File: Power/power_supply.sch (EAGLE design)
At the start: 7 parts

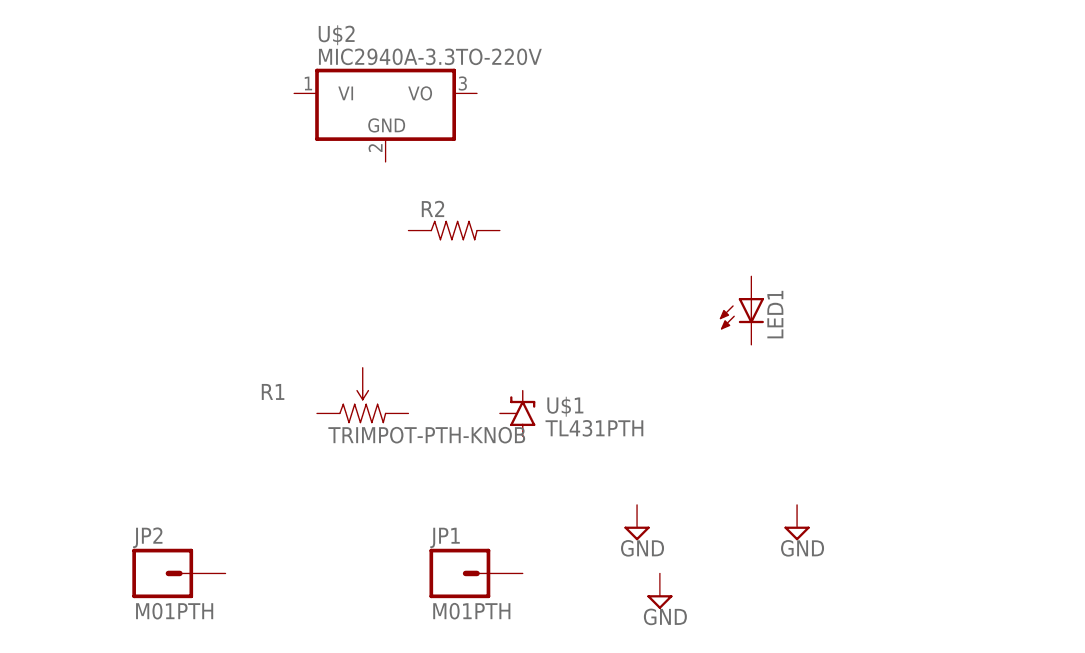
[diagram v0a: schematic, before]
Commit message: Changes to the Power Supply
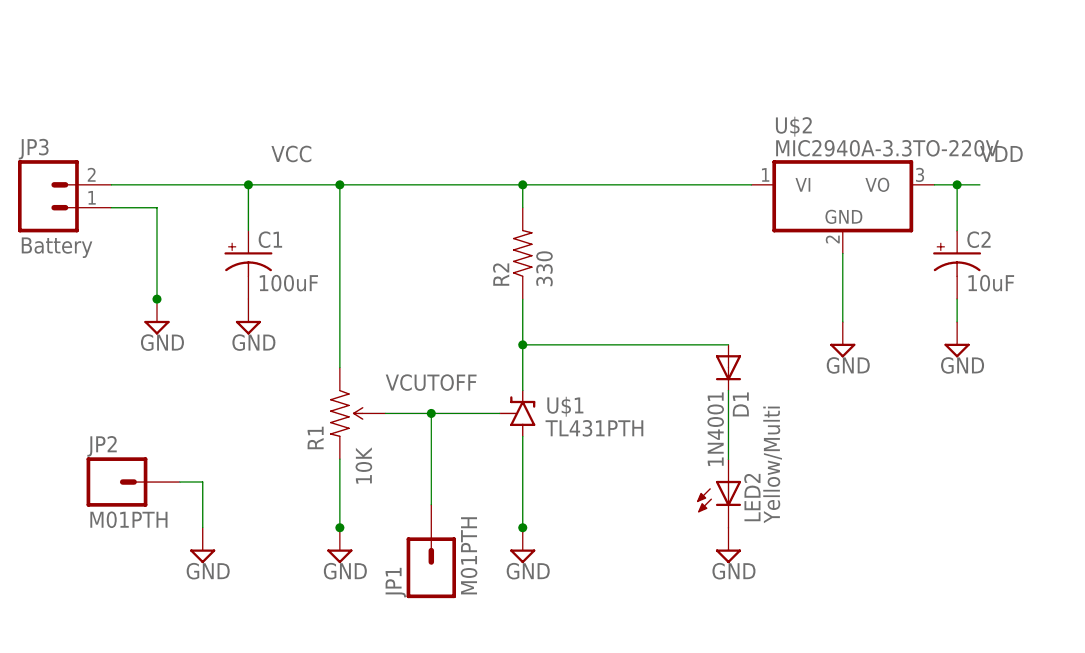
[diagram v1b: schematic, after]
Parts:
- removed LED1: (no value), SparkFun:LED10MM2
- added C1: 100uF, rcl:CPOL-USE3.5-8
- added C2: 10uF, rcl:CPOL-USE2.5-5
- added D1: 1N4001, diode:1N4004
- added JP3: Battery, SparkFun:M02PTH
- added LED2: Yellow/Multi, SparkFun:LED5MM
- R1: value TRIMPOT-PTH-KNOB -> 10K
- R2: value (none) -> 330
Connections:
- new net GND: C1.-, C2.-, JP2.1, JP3.1, LED2.C, R1.CW, U$1.A, U$2.GND
- new net N$1: D1.C, LED2.A
- new net N$2: D1.A, R2.1, U$1.C
- new net VCC: C1.+, JP3.2, R1.CCW, R2.2, U$2.VI
- new net VCUTOFF: JP1.1, R1.WIPER, U$1.R
- new net VDD: C2.+, U$2.VO
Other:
- moved on the sheet: JP1, JP2, R1, R2, U$2
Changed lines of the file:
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@@
 <layer number="97" name="Info" color="7" fill="1" visible="yes" active="yes"/>
 <layer number="98" name="Guide" color="6" fill="1" visible="yes" active="yes"/>
+<layer number="99" name="SpiceOrder" color="5" fill="1" visible="yes" active="yes"/>
 <layer number="100" name="Muster" color="7" fill="1" visible="yes" active="yes"/>
 <layer number="101" name="Patch_Top" color="7" fill="1" visible="yes" active="yes"/>
@@
 <parts>
 <part name="U$1" library="SparkFun" deviceset="TL431" device="PTH"/>
-<part name="R1" library="SparkFun" deviceset="TRIMPOT" device="-PTH-KNOB"/>
-<part name="R2" library="SparkFun" deviceset="RESISTOR" device="AXIAL-0.3"/>
+<part name="R1" library="SparkFun" deviceset="TRIMPOT" device="-PTH-KNOB" value="10K"/>
+<part name="R2" library="SparkFun" deviceset="RESISTOR" device="AXIAL-0.3" value="330"/>
 <part name="JP1" library="SparkFun" deviceset="M01" device="PTH"/>
 <part name="JP2" library="SparkFun" deviceset="M01" device="PTH"/>
-<part name="LED1" library="SparkFun" deviceset="LED" device="10MM2"/>
 <part name="SUPPLY1" library="supply2" deviceset="GND" device=""/>
 <part name="SUPPLY2" library="supply2" deviceset="GND" device=""/>
-<part name="SUPPLY3" library="supply2" deviceset="GND" device=""/>
 <part name="U$2" library="SparkFun" deviceset="MIC2940A-3.3" device="TO-220V"/>
+<part name="SUPPLY4" library="supply2" deviceset="GND" device=""/>
+<part name="SUPPLY5" library="supply2" deviceset="GND" device=""/>
+<part name="JP3" library="SparkFun" deviceset="M02" device="PTH" value="Battery"/>
+<part name="SUPPLY6" library="supply2" deviceset="GND" device=""/>
+<part name="SUPPLY7" library="supply2" deviceset="GND" device=""/>
+<part name="C1" library="rcl" deviceset="CPOL-US" device="E3.5-8" value="100uF"/>
+<part name="C2" library="rcl" deviceset="CPOL-US" device="E2.5-5" value="10uF"/>
+<part name="SUPPLY8" library="supply2" deviceset="GND" device=""/>
+<part name="SUPPLY9" library="supply2" deviceset="GND" device=""/>
+<part name="D1" library="diode" deviceset="1N4004" device="" value="1N4001"/>
+<part name="LED2" library="SparkFun" deviceset="LED" device="5MM" value="Yellow/Multi"/>
 </parts>
 <sheets>
@@
 <instances>
 <instance part="U$1" gate="G$1" x="25.4" y="12.7"/>
-<instance part="R1" gate="R?" x="7.62" y="12.7"/>
-<instance part="R2" gate="G$1" x="17.78" y="33.02"/>
-<instance part="JP1" gate="G$1" x="17.78" y="-5.08"/>
-<instance part="JP2" gate="G$1" x="-15.24" y="-5.08"/>
-<instance part="LED1" gate="G$1" x="50.8" y="25.4"/>
-<instance part="SUPPLY1" gate="GND" x="38.1" y="0"/>
-<instance part="SUPPLY2" gate="GND" x="40.64" y="-7.62"/>
-<instance part="SUPPLY3" gate="GND" x="55.88" y="0"/>
-<instance part="U$2" gate="G$1" x="10.16" y="48.26"/>
+<instance part="R1" gate="R?" x="5.08" y="12.7" smashed="yes" rot="R270">
+<attribute name="NAME" x="1.4986" y="11.43" size="1.778" layer="95" rot="R270"/>
+<attribute name="VALUE" x="6.858" y="8.89" size="1.778" layer="96" rot="R270"/>
+</instance>
+<instance part="R2" gate="G$1" x="25.4" y="30.48" rot="R90"/>
+<instance part="JP1" gate="G$1" x="15.24" y="-5.08" rot="R90"/>
+<instance part="JP2" gate="G$1" x="-20.32" y="5.08"/>
+<instance part="SUPPLY1" gate="GND" x="-10.16" y="-2.54"/>
+<instance part="SUPPLY2" gate="GND" x="5.08" y="-2.54"/>
+<instance part="U$2" gate="G$1" x="60.96" y="38.1"/>
+<instance part="SUPPLY4" gate="GND" x="25.4" y="-2.54"/>
+<instance part="SUPPLY5" gate="GND" x="48.26" y="-2.54"/>
+<instance part="JP3" gate="G$1" x="-27.94" y="35.56"/>
+<instance part="SUPPLY6" gate="GND" x="-15.24" y="22.86"/>
+<instance part="SUPPLY7" gate="GND" x="60.96" y="20.32"/>
+<instance part="C1" gate="G$1" x="-5.08" y="30.48"/>
+<instance part="C2" gate="G$1" x="73.66" y="30.48"/>
+<instance part="SUPPLY8" gate="GND" x="-5.08" y="22.86"/>
+<instance part="SUPPLY9" gate="GND" x="73.66" y="20.32"/>
+<instance part="D1" gate="1" x="48.26" y="17.78" rot="R270"/>
+<instance part="LED2" gate="G$1" x="48.26" y="5.08"/>
 </instances>
 <busses>
 </busses>
 <nets>
+<net name="GND" class="0">
+<segment>
+<pinref part="JP2" gate="G$1" pin="1"/>
+<pinref part="SUPPLY1" gate="GND" pin="GND"/>
+<wire x1="-12.7" y1="5.08" x2="-10.16" y2="5.08" width="0.1524" layer="91"/>
+<wire x1="-10.16" y1="5.08" x2="-10.16" y2="0" width="0.1524" layer="91"/>
+</segment>
+<segment>
+<pinref part="SUPPLY4" gate="GND" pin="GND"/>
+<pinref part="U$1" gate="G$1" pin="A"/>
+<wire x1="25.4" y1="10.16" x2="25.4" y2="0" width="0.1524" layer="91"/>
+<junction x="25.4" y="0"/>
+</segment>
+<segment>
+<pinref part="R1" gate="R?" pin="CW"/>
+<pinref part="SUPPLY2" gate="GND" pin="GND"/>
+<wire x1="5.08" y1="7.62" x2="5.08" y2="0" width="0.1524" layer="91"/>
+<junction x="5.08" y="0"/>
+</segment>
+<segment>
+<pinref part="JP3" gate="G$1" pin="1"/>
+<wire x1="-20.32" y1="35.56" x2="-15.24" y2="35.56" width="0.1524" layer="91"/>
+<pinref part="SUPPLY6" gate="GND" pin="GND"/>
+<wire x1="-15.24" y1="35.56" x2="-15.24" y2="25.4" width="0.1524" layer="91"/>
+<junction x="-15.24" y="25.4"/>
+</segment>
+<segment>
+<pinref part="U$2" gate="G$1" pin="GND"/>
+<pinref part="SUPPLY7" gate="GND" pin="GND"/>
+<wire x1="60.96" y1="30.48" x2="60.96" y2="22.86" width="0.1524" layer="91"/>
+</segment>
+<segment>
+<pinref part="C1" gate="G$1" pin="-"/>
+<pinref part="SUPPLY8" gate="GND" pin="GND"/>
+</segment>
+<segment>
+<pinref part="C2" gate="G$1" pin="-"/>
+<pinref part="SUPPLY9" gate="GND" pin="GND"/>
+<wire x1="73.66" y1="25.4" x2="73.66" y2="22.86" width="0.1524" layer="91"/>
+</segment>
+<segment>
+<pinref part="SUPPLY5" gate="GND" pin="GND"/>
+<pinref part="LED2" gate="G$1" pin="C"/>
+</segment>
+</net>
+<net name="VCUTOFF" class="0">
+<segment>
+<pinref part="R1" gate="R?" pin="WIPER"/>
+<pinref part="U$1" gate="G$1" pin="R"/>
+<wire x1="10.16" y1="12.7" x2="15.24" y2="12.7" width="0.1524" layer="91"/>
+<pinref part="JP1" gate="G$1" pin="1"/>
+<wire x1="15.24" y1="12.7" x2="22.86" y2="12.7" width="0.1524" layer="91"/>
+<wire x1="15.24" y1="2.54" x2="15.24" y2="12.7" width="0.1524" layer="91"/>
+<label x="10.16" y="15.24" size="1.778" layer="95"/>
+<junction x="15.24" y="12.7"/>
+</segment>
+</net>
+<net name="N$2" class="0">
+<segment>
+<pinref part="R2" gate="G$1" pin="1"/>
+<pinref part="U$1" gate="G$1" pin="C"/>
+<wire x1="25.4" y1="25.4" x2="25.4" y2="20.32" width="0.1524" layer="91"/>
+<pinref part="D1" gate="1" pin="A"/>
+<wire x1="25.4" y1="20.32" x2="25.4" y2="15.24" width="0.1524" layer="91"/>
+<wire x1="48.26" y1="20.32" x2="25.4" y2="20.32" width="0.1524" layer="91"/>
+<junction x="25.4" y="20.32"/>
+</segment>
+</net>
+<net name="VCC" class="0">
+<segment>
+<pinref part="JP3" gate="G$1" pin="2"/>
+<pinref part="R2" gate="G$1" pin="2"/>
+<wire x1="-20.32" y1="38.1" x2="-5.08" y2="38.1" width="0.1524" layer="91"/>
+<wire x1="-5.08" y1="38.1" x2="5.08" y2="38.1" width="0.1524" layer="91"/>
+<wire x1="5.08" y1="38.1" x2="25.4" y2="38.1" width="0.1524" layer="91"/>
+<wire x1="25.4" y1="38.1" x2="25.4" y2="35.56" width="0.1524" layer="91"/>
+<pinref part="R1" gate="R?" pin="CCW"/>
+<wire x1="5.08" y1="17.78" x2="5.08" y2="38.1" width="0.1524" layer="91"/>
+<pinref part="U$2" gate="G$1" pin="VI"/>
+<wire x1="25.4" y1="38.1" x2="50.8" y2="38.1" width="0.1524" layer="91"/>
+<label x="-2.54" y="40.64" size="1.778" layer="95"/>
+<pinref part="C1" gate="G$1" pin="+"/>
+<wire x1="-5.08" y1="33.02" x2="-5.08" y2="38.1" width="0.1524" layer="91"/>
+<junction x="-5.08" y="38.1"/>
+<junction x="5.08" y="38.1"/>
+<junction x="25.4" y="38.1"/>
+</segment>
+</net>
+<net name="VDD" class="0">
+<segment>
+<pinref part="U$2" gate="G$1" pin="VO"/>
+<wire x1="71.12" y1="38.1" x2="73.66" y2="38.1" width="0.1524" layer="91"/>
+<label x="76.2" y="40.64" size="1.778" layer="95"/>
+<pinref part="C2" gate="G$1" pin="+"/>
+<wire x1="73.66" y1="38.1" x2="76.2" y2="38.1" width="0.1524" layer="91"/>
+<wire x1="73.66" y1="33.02" x2="73.66" y2="38.1" width="0.1524" layer="91"/>
+<junction x="73.66" y="38.1"/>
+</segment>
+</net>
+<net name="N$1" class="0">
+<segment>
+<pinref part="D1" gate="1" pin="C"/>
+<wire x1="48.26" y1="15.24" x2="48.26" y2="7.62" width="0.1524" layer="91"/>
+<pinref part="LED2" gate="G$1" pin="A"/>
+</segment>
+</net>
 </nets>
 </sheet>

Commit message: Updated the POT package
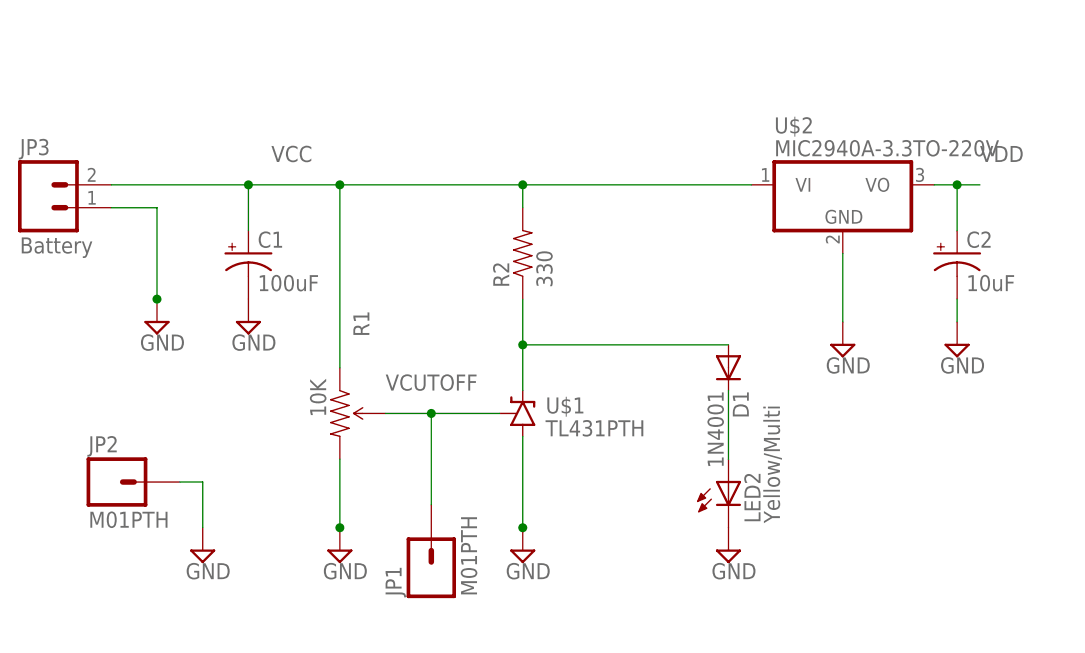
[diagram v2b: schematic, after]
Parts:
- R1: device SparkFun:TRIMPOT-PTH-KNOB -> Power:TRIMPOT-PTH-KNOB
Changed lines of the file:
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@@
 <parts>
 <part name="U$1" library="SparkFun" deviceset="TL431" device="PTH"/>
-<part name="R1" library="SparkFun" deviceset="TRIMPOT" device="-PTH-KNOB" value="10K"/>
 <part name="R2" library="SparkFun" deviceset="RESISTOR" device="AXIAL-0.3" value="330"/>
 <part name="JP1" library="SparkFun" deviceset="M01" device="PTH"/>
@@
 <part name="D1" library="diode" deviceset="1N4004" device="" value="1N4001"/>
 <part name="LED2" library="SparkFun" deviceset="LED" device="5MM" value="Yellow/Multi"/>
+<part name="R1" library="Power" deviceset="TRIMPOT" device="-PTH-KNOB" value="10K"/>
 </parts>
 <sheets>
@@
 <instances>
 <instance part="U$1" gate="G$1" x="25.4" y="12.7"/>
-<instance part="R1" gate="R?" x="5.08" y="12.7" smashed="yes" rot="R270">
-<attribute name="NAME" x="1.4986" y="11.43" size="1.778" layer="95" rot="R270"/>
-<attribute name="VALUE" x="6.858" y="8.89" size="1.778" layer="96" rot="R270"/>
-</instance>
 <instance part="R2" gate="G$1" x="25.4" y="30.48" rot="R90"/>
 <instance part="JP1" gate="G$1" x="15.24" y="-5.08" rot="R90"/>
@@
 <instance part="D1" gate="1" x="48.26" y="17.78" rot="R270"/>
 <instance part="LED2" gate="G$1" x="48.26" y="5.08"/>
+<instance part="R1" gate="R?" x="5.08" y="12.7" rot="R270"/>
 </instances>
 <busses>
@@
 </segment>
 <segment>
-<pinref part="R1" gate="R?" pin="CW"/>
 <pinref part="SUPPLY2" gate="GND" pin="GND"/>
 <wire x1="5.08" y1="7.62" x2="5.08" y2="0" width="0.1524" layer="91"/>
 <junction x="5.08" y="0"/>
+<pinref part="R1" gate="R?" pin="CW"/>
 </segment>
 <segment>
@@
 <net name="VCUTOFF" class="0">
 <segment>
-<pinref part="R1" gate="R?" pin="WIPER"/>
 <pinref part="U$1" gate="G$1" pin="R"/>
 <wire x1="10.16" y1="12.7" x2="15.24" y2="12.7" width="0.1524" layer="91"/>
@@
 <label x="10.16" y="15.24" size="1.778" layer="95"/>
 <junction x="15.24" y="12.7"/>
+<pinref part="R1" gate="R?" pin="WIPER"/>
 </segment>
 </net>
@@
 <wire x1="5.08" y1="38.1" x2="25.4" y2="38.1" width="0.1524" layer="91"/>
 <wire x1="25.4" y1="38.1" x2="25.4" y2="35.56" width="0.1524" layer="91"/>
-<pinref part="R1" gate="R?" pin="CCW"/>
 <wire x1="5.08" y1="17.78" x2="5.08" y2="38.1" width="0.1524" layer="91"/>
 <pinref part="U$2" gate="G$1" pin="VI"/>
@@
 <junction x="5.08" y="38.1"/>
 <junction x="25.4" y="38.1"/>
+<pinref part="R1" gate="R?" pin="CCW"/>
 </segment>
 </net>
